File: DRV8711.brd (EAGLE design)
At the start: 66.5 x 53.5 mm, 37 parts, among them IC1 DRV8711, T1 IPC50N04S5, T2 IPC50N04S5, T3 IPC50N04S5, T4 IPC50N04S5, T5 IPC50N04S5, T6 IPC50N04S5, T7 IPC50N04S5, T8 IPC50N04S5

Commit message: Add files via upload
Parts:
- removed JP2: (no value), pinhead:1X03
- added R17, R18, R19: 0R, rcl:R0805
- added STALL/BEMF: (no value), pinhead:1X03
- moved X2 0.77 mm to (62.1, 22.5), turned to 270 degrees
- moved COM 0.09 mm to (55.1, 16.5)
- moved CONTROL 0.09 mm to (55.1, 5.74)
- moved IC1 0.09 mm to (33.5, 11.4)
- moved R15 0.09 mm to (44.6, 9.49)
- moved R16 0.09 mm to (41.3, 9.49)
- moved C3 0.09 mm to (24.3, 12.7)
- moved C4 0.09 mm to (24.3, 10.2)
- moved X1 0.09 mm to (11.3, 11.7)
- moved C5 0.09 mm to (28.6, 2.75)
- moved C1 0.09 mm to (27.1, 6.48)
- moved C2 0.09 mm to (24.3, 2.73)
- moved R1 0.09 mm to (12.3, 30.7)
- moved R12 0.09 mm to (28.8, 31.7)
- moved R2 0.09 mm to (14.8, 30.7)
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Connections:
- net +5V: now also STALL/BEMF.1; no longer JP2.1
- net AGND: now also R17.1, R18.1, R19.1, X2.1
- net FAULT: now also STALL/BEMF.3; no longer JP2.3
- net GND: now also R17.2, R18.2, R19.2; no longer X2.1
- net STALL: now also STALL/BEMF.2; no longer JP2.2
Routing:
- net V+: track 187.6 -> 123.3 mm, vias 3 -> 10
- net AGND: track 79.5 -> 35.1 mm, vias 3 -> 16
- net B2LS: track 34.7 -> 35.7 mm
- net B2HS: track 52.3 -> 52.8 mm
- net GND: vias 12 -> 20
- added copper zone on layer 1, net AGND
- added copper zone on layer 16, net AGND
- added copper zone on layer 1, net V+
- added copper zone on layer 16, net V+
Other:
- board size 66.5 x 53.5 mm -> 66.8 x 53.5 mm
- board text added: "+"
- board text added: "-"

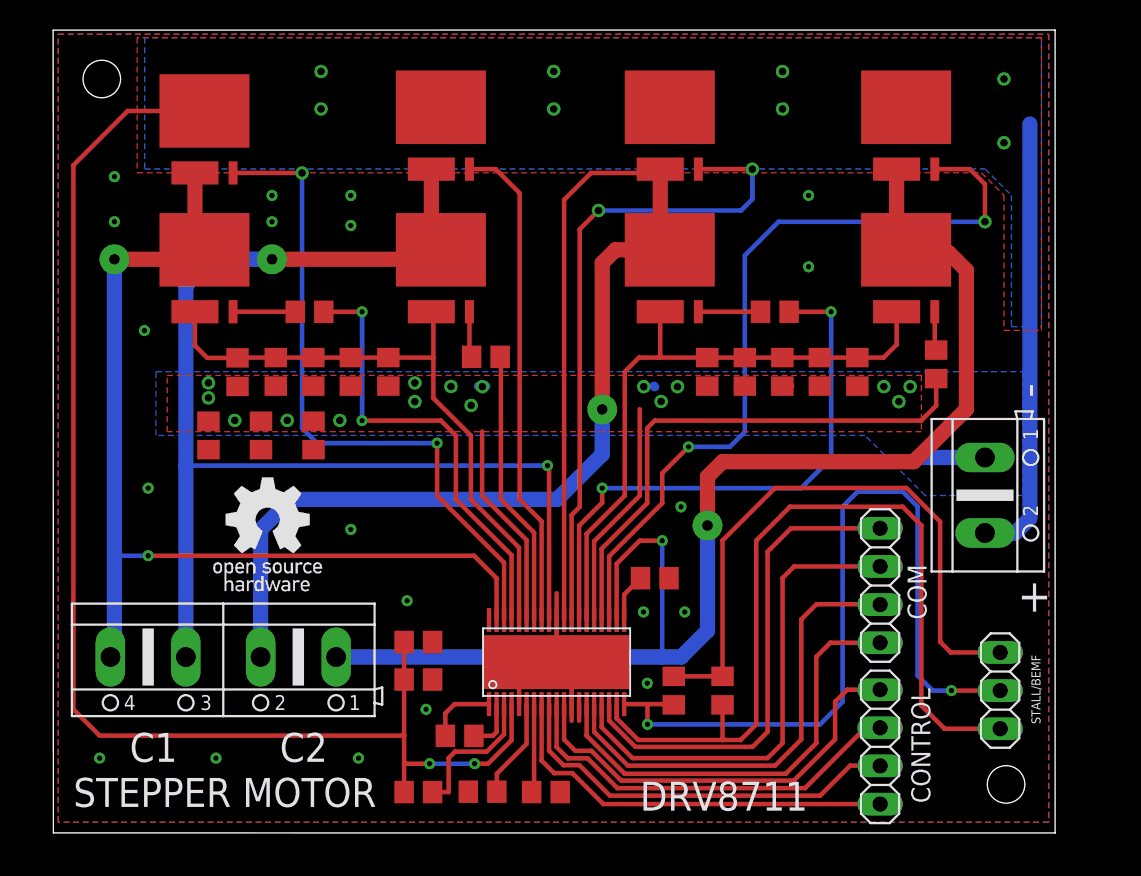
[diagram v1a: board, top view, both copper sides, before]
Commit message: Add files via upload
without 5 parallel resistors
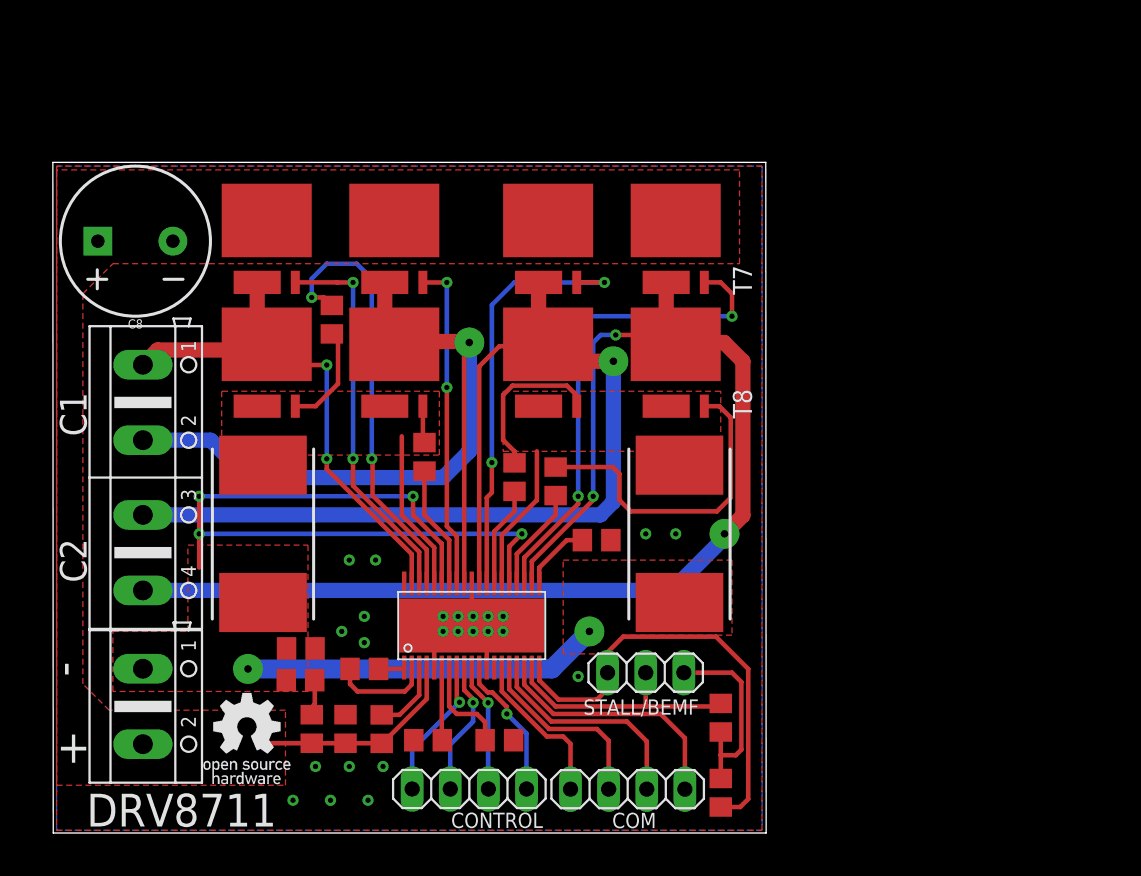
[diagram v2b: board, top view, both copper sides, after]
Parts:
- removed R10, R11, R3, R4, R5, R7, R8, R9: (no value), rcl:R0805
- removed R19: 0R, rcl:R0805
- added C8: 1mF, SparkFun-Capacitors:CPOL-RADIAL-5MM-10MM
- R1, R2: value (none) -> 0.05R/5W; device rcl:R0805 -> rcl:R4527
- moved X2 57.8 mm to (5.97, 8.43)
- moved R2 29.0 mm to (41.7, 19.9)
- moved CONTROL 27.5 mm to (27.7, 2.93), turned to 180 degrees
- moved R14 26.5 mm to (33.5, 23.4)
- moved STALL/BEMF 23.6 mm to (39.5, 10.7), turned to 180 degrees
- moved COM 21.6 mm to (38.3, 2.92), turned to 180 degrees
- moved R13 20.5 mm to (30.7, 23.7), turned to 90 degrees
- moved T7 17.1 mm to (41.5, 39.7)
- moved T8 16.6 mm to (41.5, 31.4)
- moved R18 16.3 mm to (16.5, 10.2), turned to 0 degrees
- moved R17 15.5 mm to (16.5, 12.3), turned to 0 degrees
- moved X1 13.1 mm to (5.97, 23.7), turned to 270 degrees
- moved T5 11.1 mm to (33.0, 39.7)
- moved R1 10.9 mm to (14.0, 19.9)
- moved T6 10.3 mm to (33.0, 31.4)
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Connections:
- net AGND: no longer R10.1, R11.1, R19.1, R3.1, R4.1, R5.1, R7.1, R8.1, R9.1
- net AISENP: no longer R2.2, R3.2, R4.2, R5.2
- net AOUT1: now also X1.1; no longer X1.4
- net AOUT2: now also X1.2; no longer X1.3
- net BISENP: now also R2.2; no longer R10.2, R11.2, R7.2, R8.2, R9.2
- net BOUT1: now also X1.3; no longer X1.2
- net BOUT2: now also X1.4; no longer X1.1
- net FAULT: now also STALL/BEMF.2; no longer STALL/BEMF.3
- net GND: now also C8.-; no longer R19.2
- net STALL: now also STALL/BEMF.3; no longer STALL/BEMF.2
- net V+: now also C8.+
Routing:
- net V+: track 123.3 -> 14.5 mm, vias 10 -> 0
- net FAULT: track 56.2 -> 16.6 mm
- net AGND: track 35.1 -> 74.5 mm, vias 16 -> 6
- net BISENP: track 41.8 -> 9.78 mm
- net AOUT1: track 67.6 -> 36.1 mm
- net B1LS: track 38.1 -> 6.70 mm, vias 2 -> 0
- net AISENP: track 41.5 -> 10.7 mm
- net B2LS: track 35.7 -> 6.93 mm
- net +5V: track 41.5 -> 13.2 mm
- net AOUT2: track 83.2 -> 58.3 mm, vias 2 -> 1
- net STALL: track 54.3 -> 30.1 mm, vias 2 -> 0
- net BOUT1: track 93.1 -> 70.4 mm
- net B2HS: track 52.8 -> 32.8 mm
- net N$1: track 2.59 -> 21.7 mm
- net SCLK: track 29.7 -> 10.6 mm
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- added copper zone on layer 1, net AISENP
- added copper zone on layer 1, net BISENP
- removed copper zone on layer 16, net AGND
- removed copper zone on layer 16, net V+
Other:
- board size 66.8 x 53.5 mm -> 47.5 x 44.7 mm
- board text removed: "STEPPER MOTOR"

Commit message: Add files via upload
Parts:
- R1, R2: value 0.05R/5W -> 0.3R/2W; device rcl:R4527 -> rcl:R2512
- moved R2 0.98 mm to (40.8, 20.0)
- moved R1 0.07 mm to (14.0, 20.0)
